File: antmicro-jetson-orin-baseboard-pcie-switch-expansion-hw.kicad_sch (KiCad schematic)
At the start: 10 parts

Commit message: [#100765] Update schematic
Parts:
- A2: now left out of the parts list
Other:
- sheet Expansion Connector ports: added SEL, {I_{2}C}; removed none
- sheet PCIe Switch ports: added {JTAG}; removed none
- sheet Tag Connect, EEPROM ports: added {JTAG}; removed none
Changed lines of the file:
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@@
 	(wire
 		(pts
-			(xy 229.87 99.06) (xy 232.41 99.06)
+			(xy 229.87 102.87) (xy 236.22 102.87)
+		)
+		(stroke
+			(width 0)
+			(type default)
+		)
+	)
+	(bus
+		(pts
+			(xy 251.46 101.6) (xy 256.54 101.6)
 		)
 		(stroke
@@
 	(bus
 		(pts
+			(xy 247.65 95.25) (xy 247.65 106.68)
+		)
+		(stroke
+			(width 0)
+			(type default)
+		)
+	)
+	(bus
+		(pts
 			(xy 332.74 116.84) (xy 336.55 116.84)
 		)
@@
 		)
 	)
+	(bus
+		(pts
+			(xy 247.65 106.68) (xy 256.54 106.68)
+		)
+		(stroke
+			(width 0)
+			(type default)
+		)
+	)
 	(wire
 		(pts
-			(xy 232.41 116.84) (xy 234.95 116.84)
+			(xy 236.22 127) (xy 256.54 127)
 		)
 		(stroke
@@
 		)
 	)
+	(bus
+		(pts
+			(xy 251.46 59.69) (xy 251.46 101.6)
+		)
+		(stroke
+			(width 0)
+			(type default)
+		)
+	)
+	(bus
+		(pts
+			(xy 290.83 97.79) (xy 294.64 97.79)
+		)
+		(stroke
+			(width 0)
+			(type default)
+		)
+	)
 	(wire
 		(pts
-			(xy 44.1451 260.35) (xy 41.91 260.35)
+			(xy 241.3 99.06) (xy 241.3 116.84)
 		)
 		(stroke
@@
 	(bus
 		(pts
-			(xy 290.83 97.79) (xy 294.64 97.79)
+			(xy 229.87 95.25) (xy 247.65 95.25)
 		)
 		(stroke
@@
 	(bus
 		(pts
+			(xy 257.81 59.69) (xy 251.46 59.69)
+		)
+		(stroke
+			(width 0)
+			(type default)
+		)
+	)
+	(bus
+		(pts
 			(xy 294.64 113.03) (xy 302.26 113.03)
 		)
@@
 	(wire
 		(pts
+			(xy 229.87 99.06) (xy 241.3 99.06)
+		)
+		(stroke
+			(width 0)
+			(type default)
+		)
+	)
+	(wire
+		(pts
+			(xy 241.3 116.84) (xy 302.26 116.84)
+		)
+		(stroke
+			(width 0)
+			(type default)
+		)
+	)
+	(wire
+		(pts
 			(xy 40.64 254) (xy 41.91 254)
 		)
@@
 	(wire
 		(pts
-			(xy 232.41 116.84) (xy 232.41 99.06)
+			(xy 236.22 127) (xy 236.22 102.87)
 		)
 		(stroke
@@
 		(body_style 1)
 		(exclude_from_sim no)
-		(in_bom yes)
+		(in_bom no)
 		(on_board yes)
 		(in_pos_files yes)
@@
 		)
 		(property "Value" "GND"
-			(at 40.64 275.59 0)
-			(show_name no)
-			(do_not_autoplace no)
-			(effects
-				(font
-					(size 1.27 1.27)
-					(thickness 0.15)
-				)
+			(at 43.18 271.78 0)
+			(show_name no)
+			(do_not_autoplace no)
+			(effects
+				(font
+					(size 1.27 1.27)
+					(thickness 0.15)
+				)
+				(justify left)
 			)
 		)
@@
 	(sheet
 		(at 256.54 86.36)
-		(size 34.29 16.51)
+		(size 34.29 24.13)
 		(exclude_from_sim no)
 		(in_bom yes)
@@
 		)
 		(property "Sheetfile" "pcie-switch.kicad_sch"
-			(at 256.54 103.4546 0)
+			(at 256.54 111.0746 0)
 			(show_name no)
 			(do_not_autoplace no)
@@
 		)
 		(pin "{I_{2}C}" bidirectional
-			(at 270.51 102.87 270)
+			(at 256.54 106.68 180)
 			(effects
 				(font
@@
 		(pin "{SPI}" bidirectional
 			(at 256.54 97.79 180)
+			(effects
+				(font
+					(size 1.27 1.27)
+				)
+				(justify left)
+			)
+		)
+		(pin "{JTAG}" bidirectional
+			(at 256.54 101.6 180)
 			(effects
 				(font
@@
 			)
 		)
+		(pin "{JTAG}" bidirectional
+			(at 257.81 59.69 180)
+			(effects
+				(font
+					(size 1.27 1.27)
+				)
+				(justify left)
+			)
+		)
 		(instances
 			(project "antmicro-jetson-orin-baseboard-pcie-switch-expansion-hw"
@@
 	)
 	(sheet
-		(at 234.95 113.03)
+		(at 256.54 123.19)
 		(size 19.05 12.7)
 		(exclude_from_sim no)
@@
 		)
 		(property "Sheetname" "Supply"
-			(at 234.95 112.3184 0)
+			(at 256.54 122.4784 0)
 			(show_name no)
 			(do_not_autoplace no)
@@
 		)
 		(property "Sheetfile" "supply.kicad_sch"
-			(at 234.95 126.3146 0)
+			(at 256.54 136.4746 0)
 			(show_name no)
 			(do_not_autoplace no)
@@
 		)
 		(pin "POWER_EN" input
-			(at 234.95 116.84 180)
+			(at 256.54 127 180)
 			(effects
 				(font
@@
 	(sheet
 		(at 200.66 86.36)
-		(size 29.21 16.51)
+		(size 29.21 19.05)
 		(exclude_from_sim no)
 		(in_bom yes)
@@
 		)
 		(property "Sheetfile" "expansion-conn.kicad_sch"
-			(at 200.66 103.4546 0)
+			(at 200.66 105.9946 0)
 			(show_name no)
 			(do_not_autoplace no)
@@
 		)
 		(pin "POWER_EN" output
-			(at 229.87 99.06 0)
+			(at 229.87 102.87 0)
 			(effects
 				(font
@@
 			(effects
 				(font
+					(size 1.27 1.27)
+				)
+				(justify right)
+			)
+		)
+		(pin "{I_{2}C}" bidirectional
+			(at 229.87 95.25 0)
+			(effects
+				(font
+					(size 1.27 1.27)
+				)
+				(justify right)
+			)
+		)
+		(pin "SEL" input
+			(at 229.87 99.06 0)
+			(effects
+				(font

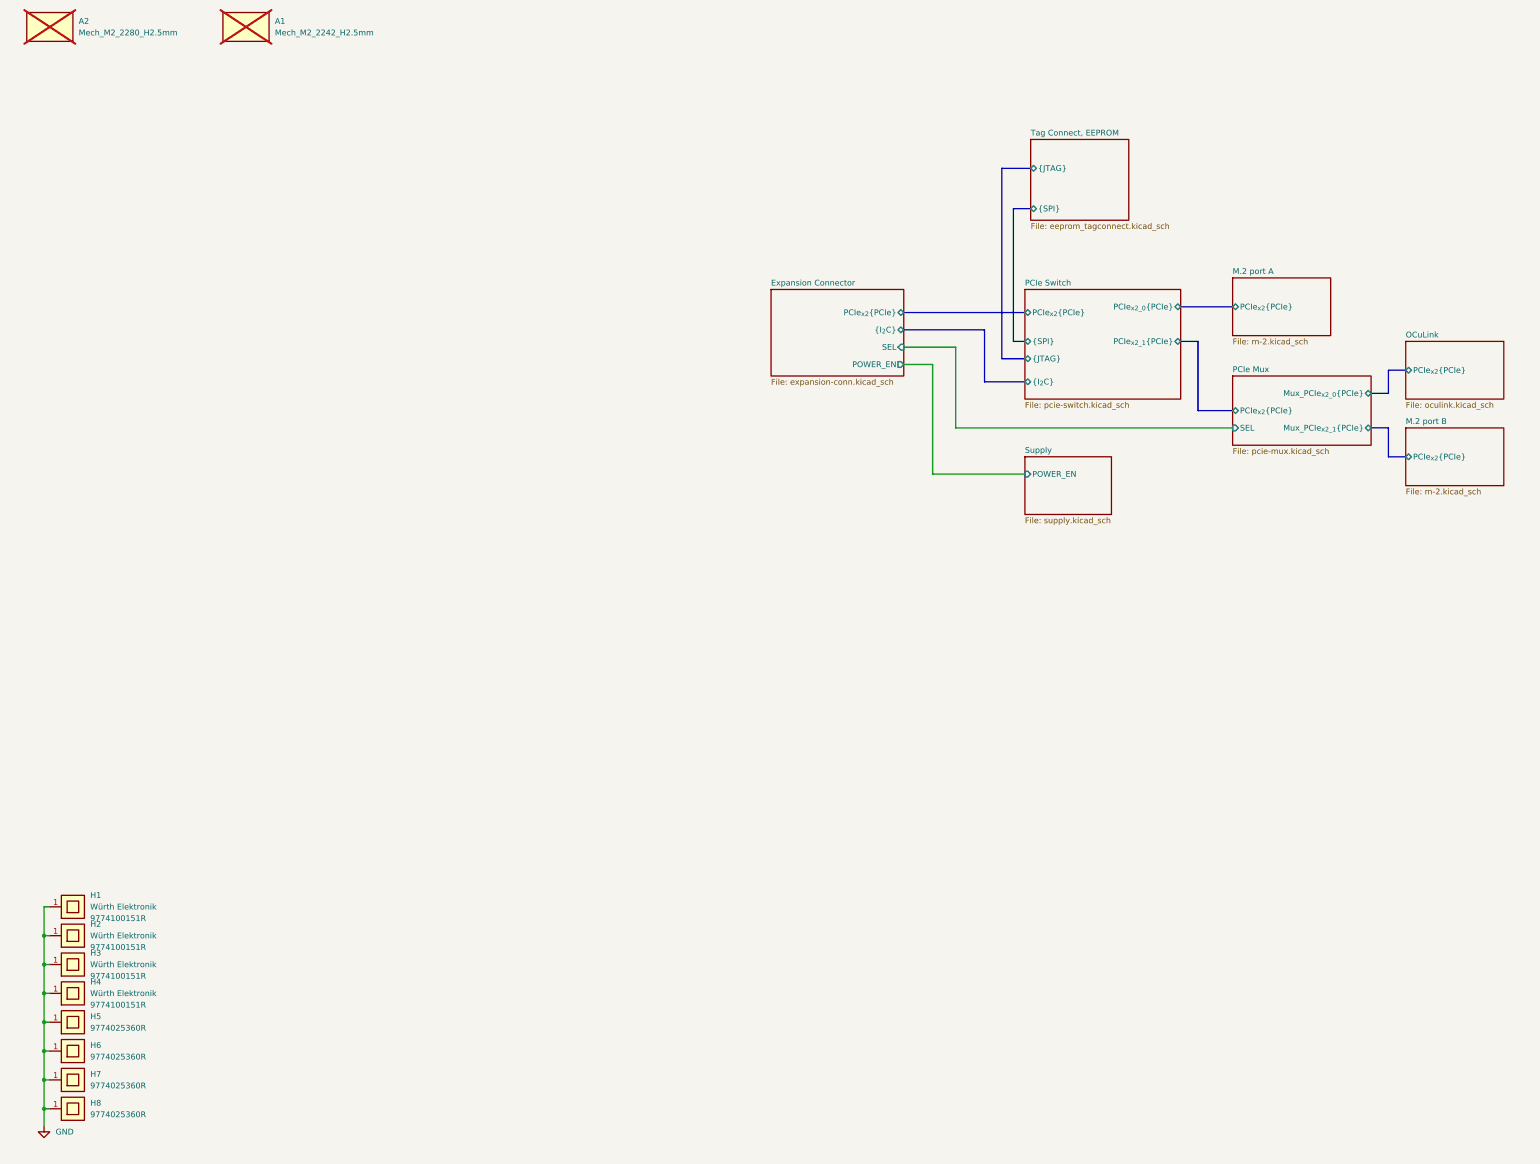
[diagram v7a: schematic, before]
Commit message: [#100765] Change sheet format to A3, update schematic
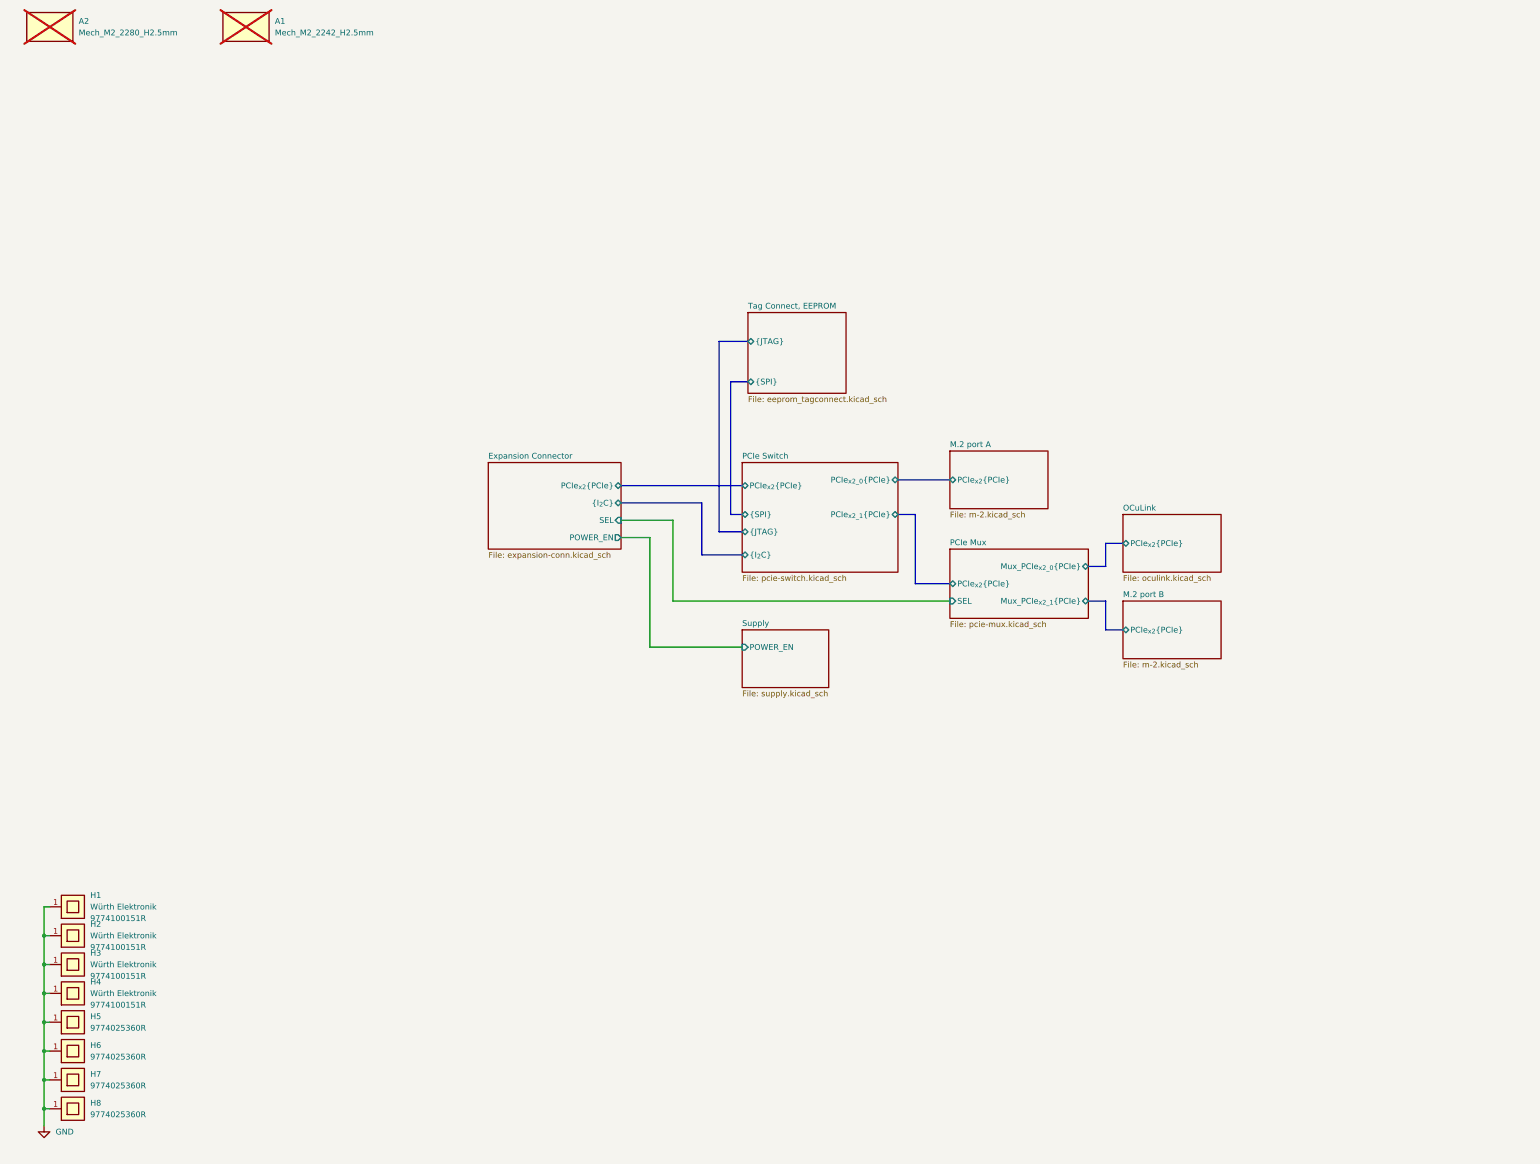
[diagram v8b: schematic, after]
